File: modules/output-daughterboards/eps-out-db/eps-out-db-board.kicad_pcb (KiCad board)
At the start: 4 copper layers, 109.5 x 67 mm, 11 parts, among them J1 EPS8 OUT FIELD, J10 TE 63849-1, J11 TE 63849-1, J12 TE 63849-1, J13 TE 63849-1, J14 TE 63849-1, J15 TE 63849-1

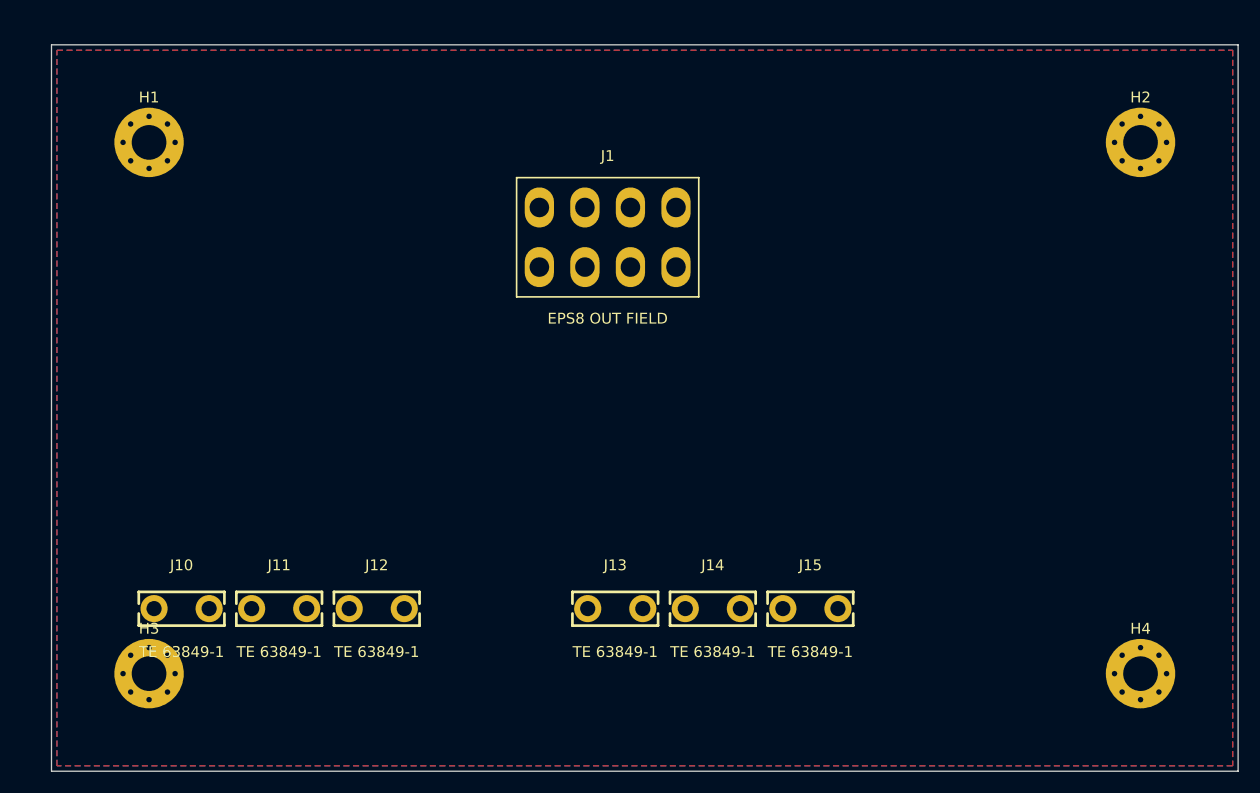
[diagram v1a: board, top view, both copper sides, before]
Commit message: Bench-mode Max addendum: T1 carries continuous telemetry, bursts for raw; GOWIN+P4 hub shape
Sustained budget 180-900 kB/s (10-50kHz/ch decimated) = 1.6-8% of one
100BASE-T1 link; fast-path raw-window bursts land <1s; continuous instrument
raw (100-260 MB/s at the ruled ADC options) exceeds every link class incl.
1000BASE-T1 — the ruled shape stays burst-into-memory, matching SS6.11's own
framing. Max hub ranked: GOWIN GW5A + P4 (owner prototype lineage) >
PolarFire ENT-posture variant > P4-only (OQ-20 caps N=1). GbE/RGMII egress
over USB HS at N=8. Freshness gaps corroborated (SS6.11 retired mux array +
debunked 2-5MHz band already owner-pen-tracked; phantom 'companion FPGA-Max
doc' cited 3x, absent). 8 owner questions incl. a REAL mismatch: owner fast
ADC = two CURRENT pairs (shunt+coil) vs the June-11 ruling's voltage+current
— where does the ATX-ripple VOLTAGE channel live?

Co-Authored-By: Claude Fable 5 <noreply@anthropic.com>
Claude-Session: https://claude.ai/code/session_01LvfqcnEeuin2oyJQw548EX
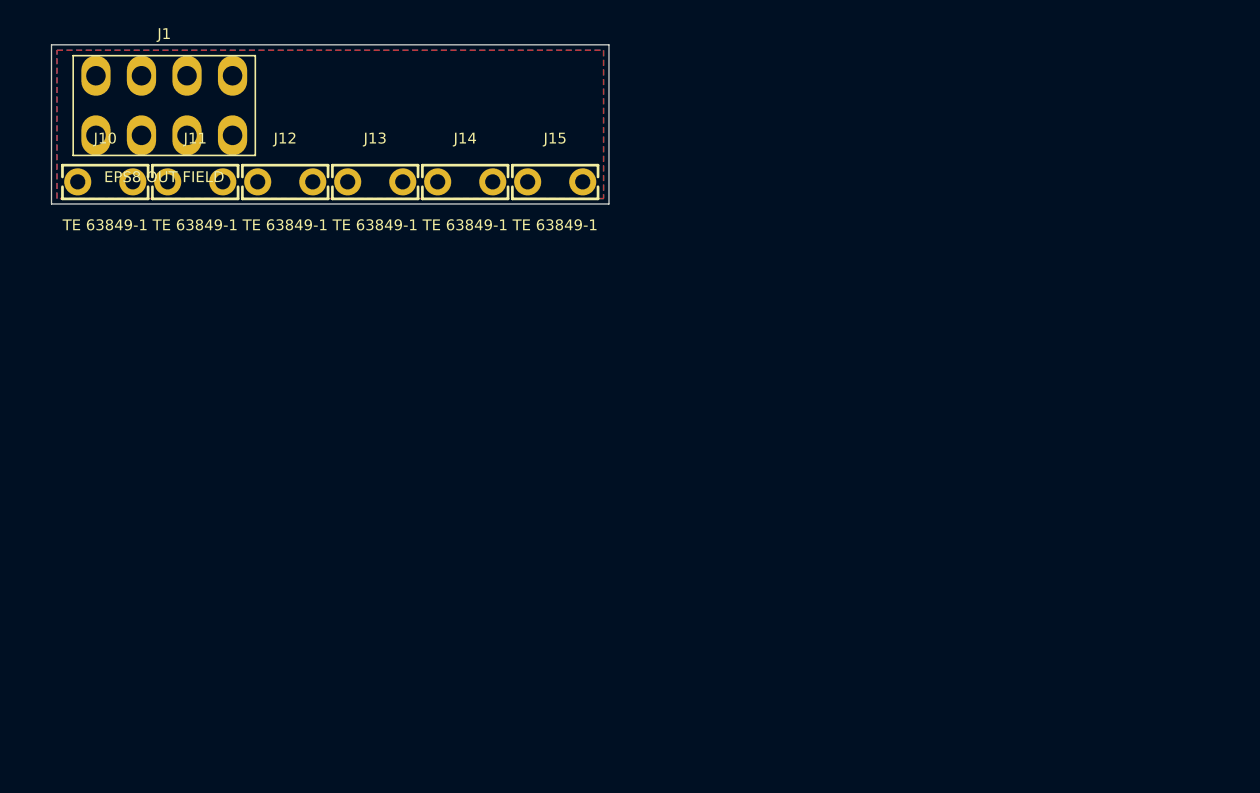
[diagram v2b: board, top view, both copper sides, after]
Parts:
- removed H1, H2, H3, H4: MountingHole_3.2mm_M3_Pad_Via, cec-MountingHole:MountingHole_3.2mm_M3_Pad_Via
- moved J15 45.9 mm to (46.5, 12.6)
- moved J14 45.5 mm to (38.2, 12.6)
- moved J13 45.2 mm to (29.9, 12.6)
- moved J1 42.7 mm to (4.10, 2.85)
- moved J12 40.3 mm to (21.6, 12.6)
- moved J11 40.1 mm to (13.3, 12.6)
- moved J10 40.0 mm to (4.96, 12.6)
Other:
- board size 109.5 x 67 mm -> 51.4 x 14.7 mm

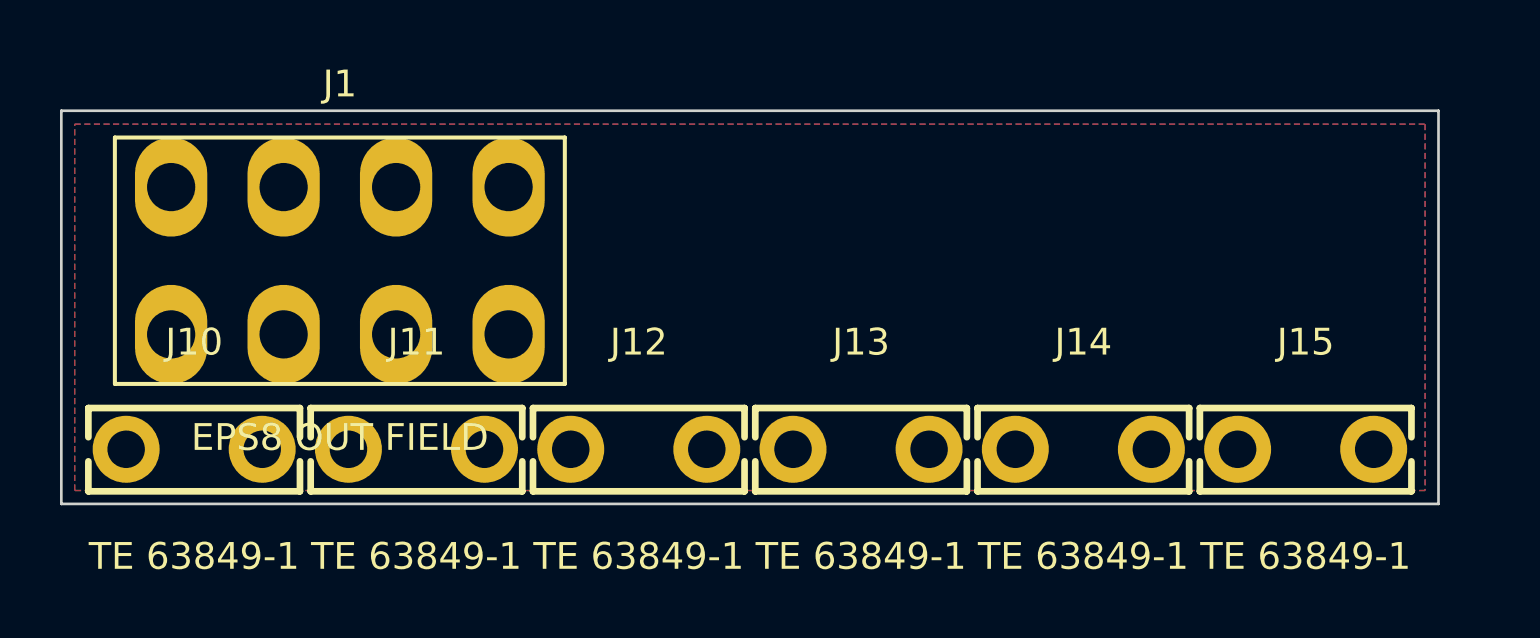
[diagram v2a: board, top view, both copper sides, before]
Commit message: Bench-mode SS7: voltage-path analysis + slow-path ceiling math (owner datasheet)
INA240 verified 400kHz -3dB flat across gains w/ 100kHz 2%-THD clean ceiling;
CSS2H R-series publishes only '<2nH' (no typ/curve) -> corner bracket
53-318kHz, consistent w/ the platform's 79.6kHz figure — BOTH caps land
~80-100kHz, neither dominates; production slow path ~1.6-2x prototype raw /
8-10x usable, gated on the OQ-21 ADC. RECOMMENDATION: fast-path VOLTAGE
(ATX ripple = the fast channel's own headline use case); across-connector
differential-V microarc observable = checked against the arc/phenomenology
corpus and NOVEL. Owner arc-recap + prototype-artifact framing recorded
verbatim; open questions extended (9-11).

Co-Authored-By: Claude Fable 5 <noreply@anthropic.com>
Claude-Session: https://claude.ai/code/session_01LvfqcnEeuin2oyJQw548EX
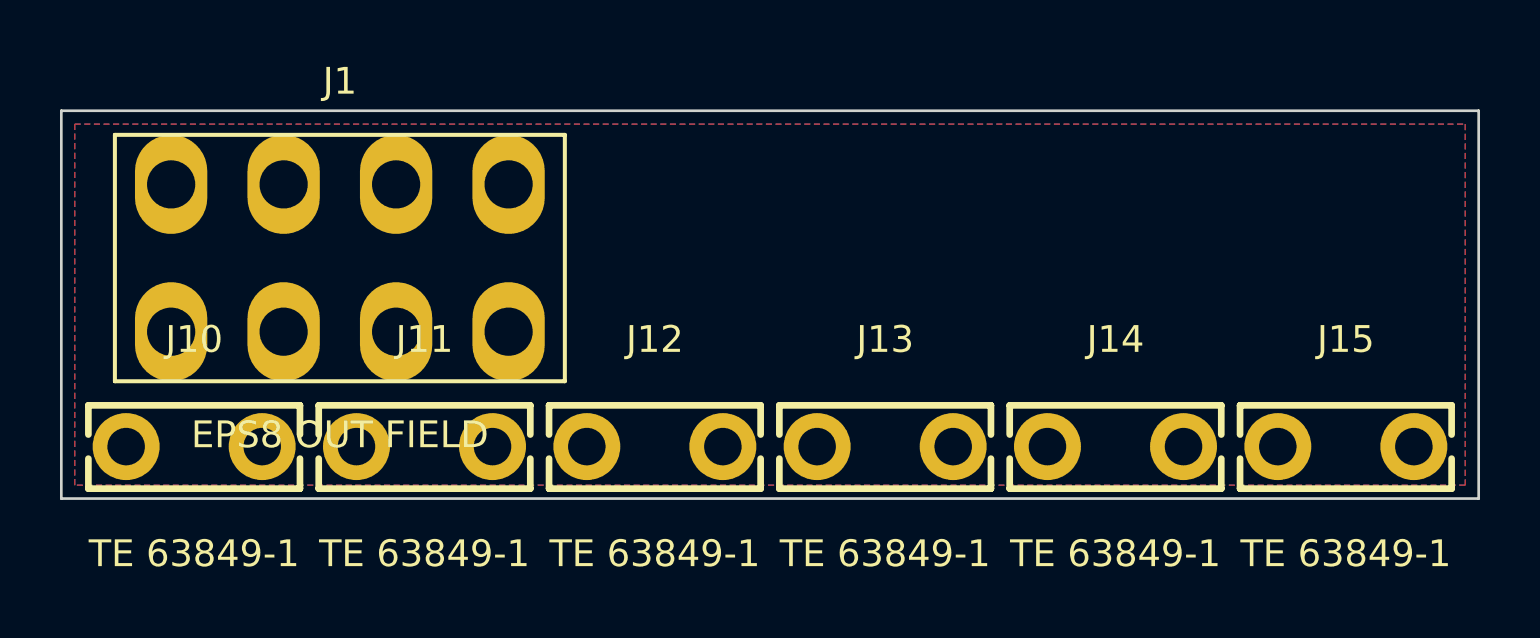
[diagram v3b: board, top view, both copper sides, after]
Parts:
- moved J15 1.50 mm to (48.0, 12.5)
- moved J14 1.20 mm to (39.4, 12.5)
- moved J13 0.91 mm to (30.8, 12.5)
- moved J12 0.61 mm to (22.2, 12.5)
- moved J11 0.32 mm to (13.6, 12.5)
- moved J10 0.10 mm to (4.96, 12.5)
- moved J1 0.10 mm to (4.10, 2.75)
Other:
- board size 51.4 x 14.7 mm -> 52.9 x 14.5 mm

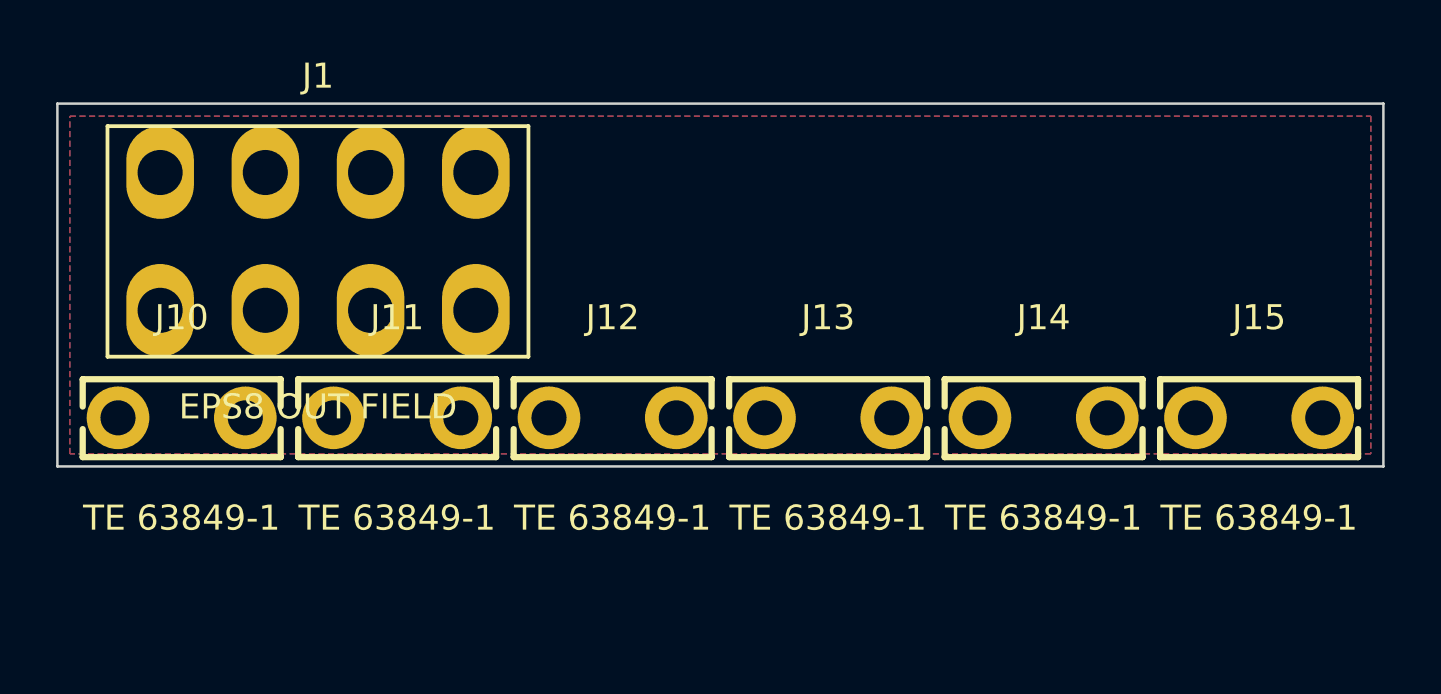
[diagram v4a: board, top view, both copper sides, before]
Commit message: WIP snapshot: flat-tab agent regenerating daughterboards onto TE 63951-1 (durability; verification pending)
Co-Authored-By: Claude Fable 5 <noreply@anthropic.com>
Claude-Session: https://claude.ai/code/session_01LvfqcnEeuin2oyJQw548EX
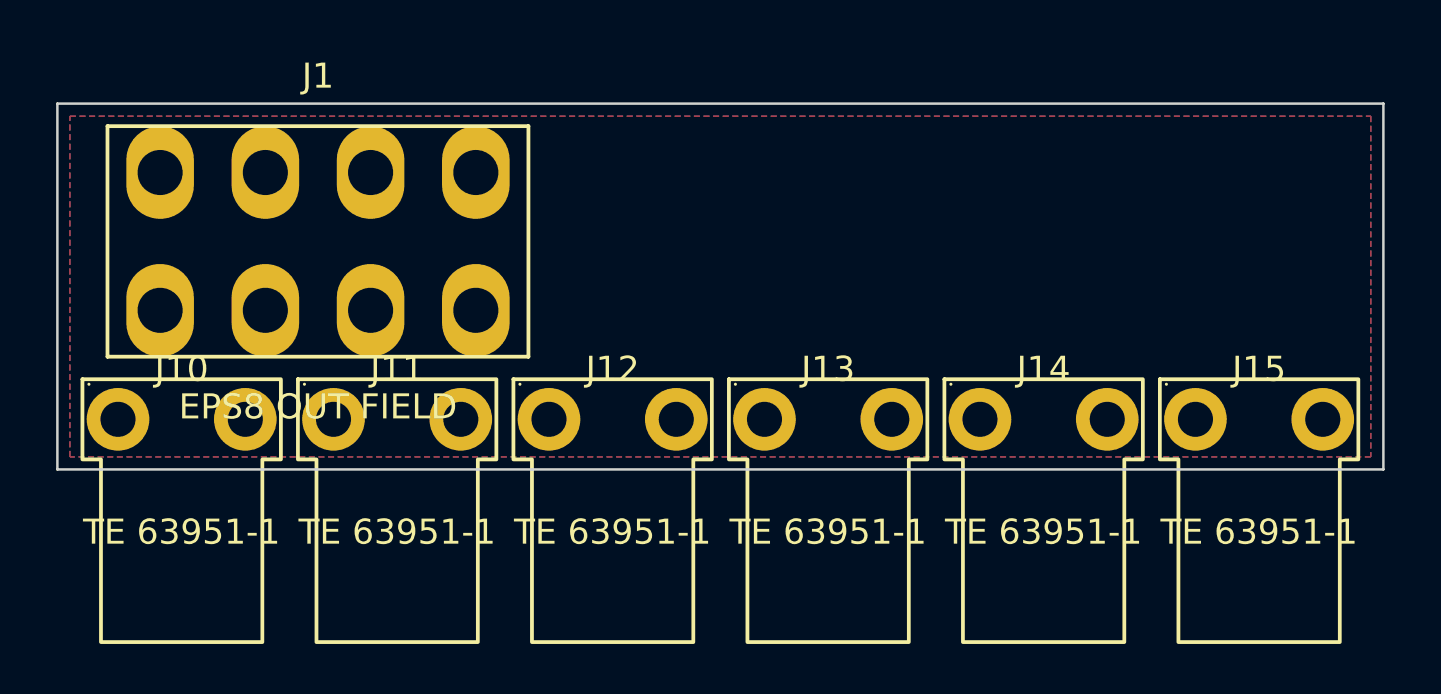
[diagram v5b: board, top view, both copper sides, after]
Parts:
- J10, J11, J12, J13, J14, J15: value TE 63849-1 -> TE 63951-1; footprint cec-Connector_Blade:TE_63849-1_FASTON_Tab_250x032_THT -> cec-Connector_Blade:TE_63951-1_FASTON_Tab_250x032_RA_THT
- moved J10 0.06 mm to (4.96, 12.6)
- moved J11 0.06 mm to (13.6, 12.6)
- moved J12 0.06 mm to (22.2, 12.6)
- moved J13 0.06 mm to (30.8, 12.6)
- moved J14 0.06 mm to (39.4, 12.6)
- moved J15 0.06 mm to (48.0, 12.6)
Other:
- board size 52.9 x 14.5 mm -> 52.9 x 14.6 mm

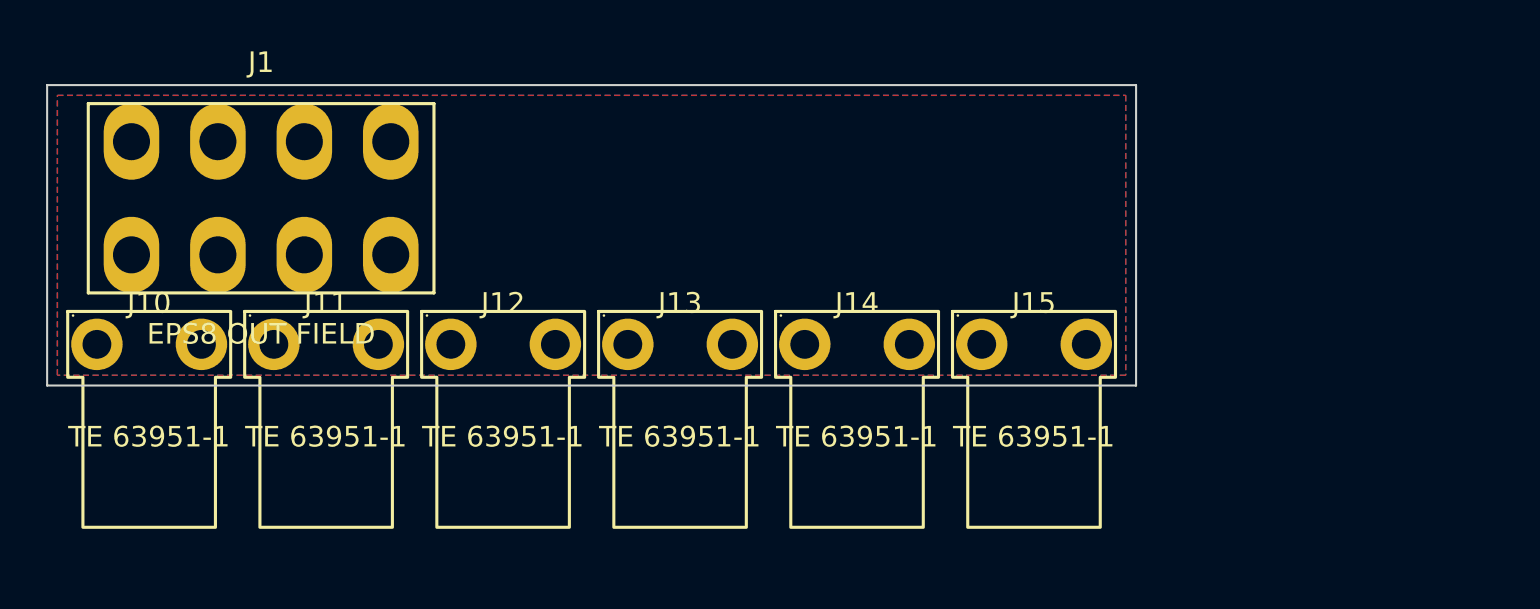
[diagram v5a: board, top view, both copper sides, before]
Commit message: Daughterboard tab form FINAL (owner sketch): 63951-1 legs-vertical, blade-down vertical drop, floating seat — all 3 boards regenerated, gates re-verified
- Part model corrected from TE dwg C=63951 (in-plane L; blade at 2.54-8.89mm face standoff, tip 15.75mm below leg midpoint)
- Boards: atx24 145.1x13.6 / eps 67.8x11.0 / pcie 49.4x11.0 (heights inside the <=15mm cap)
- Seating: board floats 8.4-11mm; full 7.16mm jaw engagement; clip slot rotated perpendicular to wall line (5.72mm standoff); row-fit margins verified at kept pitches
- Coordinator re-verified: ERC 0 x3, DRC 0/0 severity-error x3, checker fully green (incl. new orientation/uniform-height/clip-fit assertions), keying no-subset re-proved, net maps + joint counts 9/6/4 unchanged
- owner-queue: fit-check row updated to the final form; 0.27mm hang-shortfall item retired as obsolete; new sample-check items: 15.75mm chain-dim reading, top-entry drop, 0.84mm tab tolerance

Co-Authored-By: Claude Fable 5 <noreply@anthropic.com>
Claude-Session: https://claude.ai/code/session_01LvfqcnEeuin2oyJQw548EX
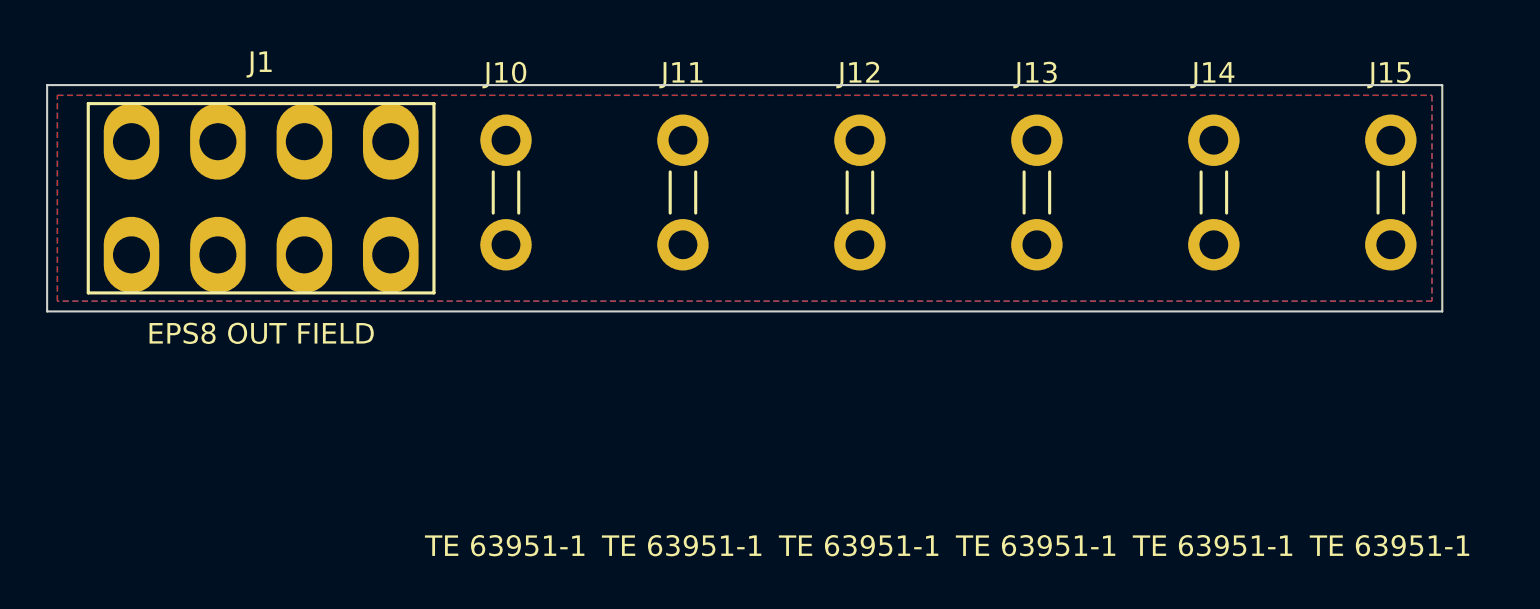
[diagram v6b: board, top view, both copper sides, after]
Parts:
- moved J14 18.8 mm to (56.7, 5.22)
- moved J10 18.8 mm to (22.3, 5.22)
- moved J12 18.8 mm to (39.5, 5.22)
- moved J13 18.8 mm to (48.1, 5.22)
- moved J11 18.8 mm to (30.9, 5.22)
- moved J15 18.8 mm to (65.3, 5.22)
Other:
- board size 52.9 x 14.6 mm -> 67.8 x 11 mm
